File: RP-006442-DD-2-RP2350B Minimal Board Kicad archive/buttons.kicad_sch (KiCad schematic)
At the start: 5 parts, among them SW10 SW_DIP_x08, SW5 SW_Push, SW6 SW_Push, SW7 SW_Push, SW8 SW_Push

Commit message: Update 8-bit switch, footprint, datasheet
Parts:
- SW10: footprint Button_Switch_SMD:SW_DIP_SPSTx08_Slide_Omron_A6S-810x_W8.9mm_P2.54mm -> Button_Switch_SMD:SW_DIP_SPSTx08_Slide_9.78x22.5mm_W8.61mm_P2.54mm
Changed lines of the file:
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@@
 			)
 		)
-		(property "Footprint" "Button_Switch_SMD:SW_DIP_SPSTx08_Slide_Omron_A6S-810x_W8.9mm_P2.54mm"
+		(property "Footprint" "Button_Switch_SMD:SW_DIP_SPSTx08_Slide_9.78x22.5mm_W8.61mm_P2.54mm"
 			(at 135.89 109.22 0)
 			(effects
@@
 			)
 		)
-		(property "Datasheet" "https://jlcpcb.com/api/file/downloadByFileSystemAccessId/8588905267774042112"
+		(property "Datasheet" "https://jlcpcb.com/partdetail/55978-DSIC08LSGET/C54953"
 			(at 135.89 109.22 0)
 			(effects

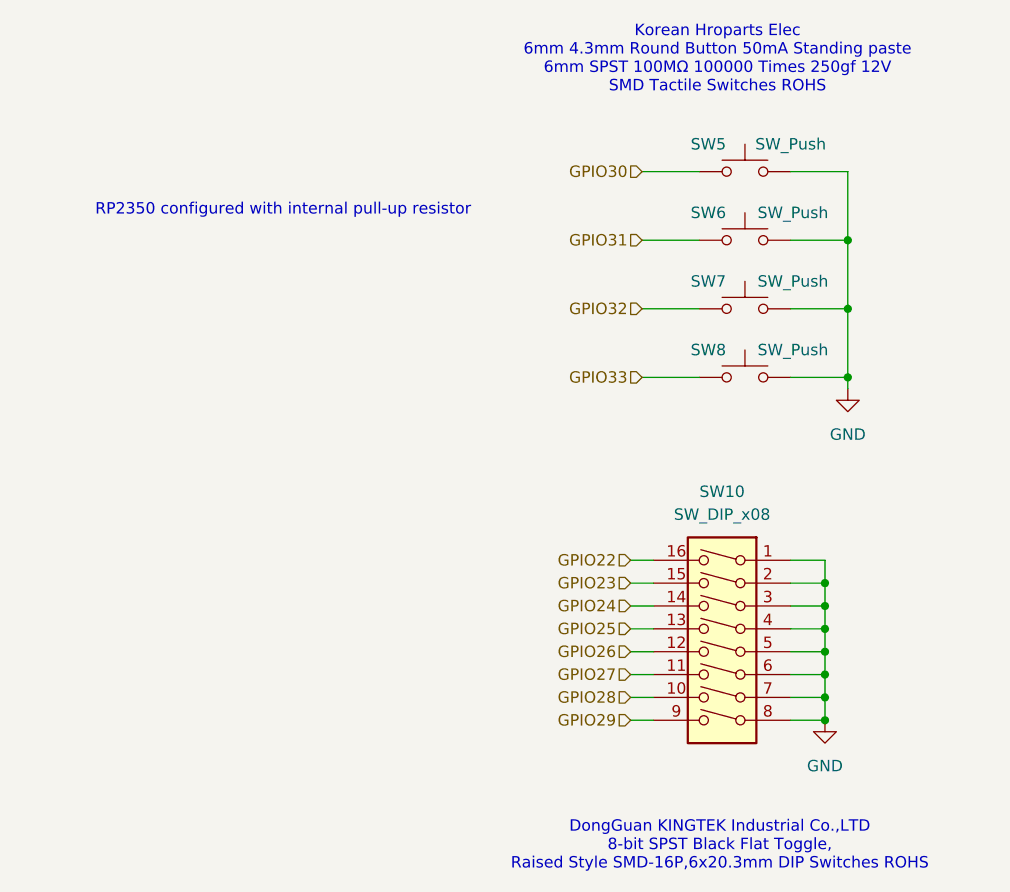
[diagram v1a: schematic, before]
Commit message: Added LCSC numbers to parts
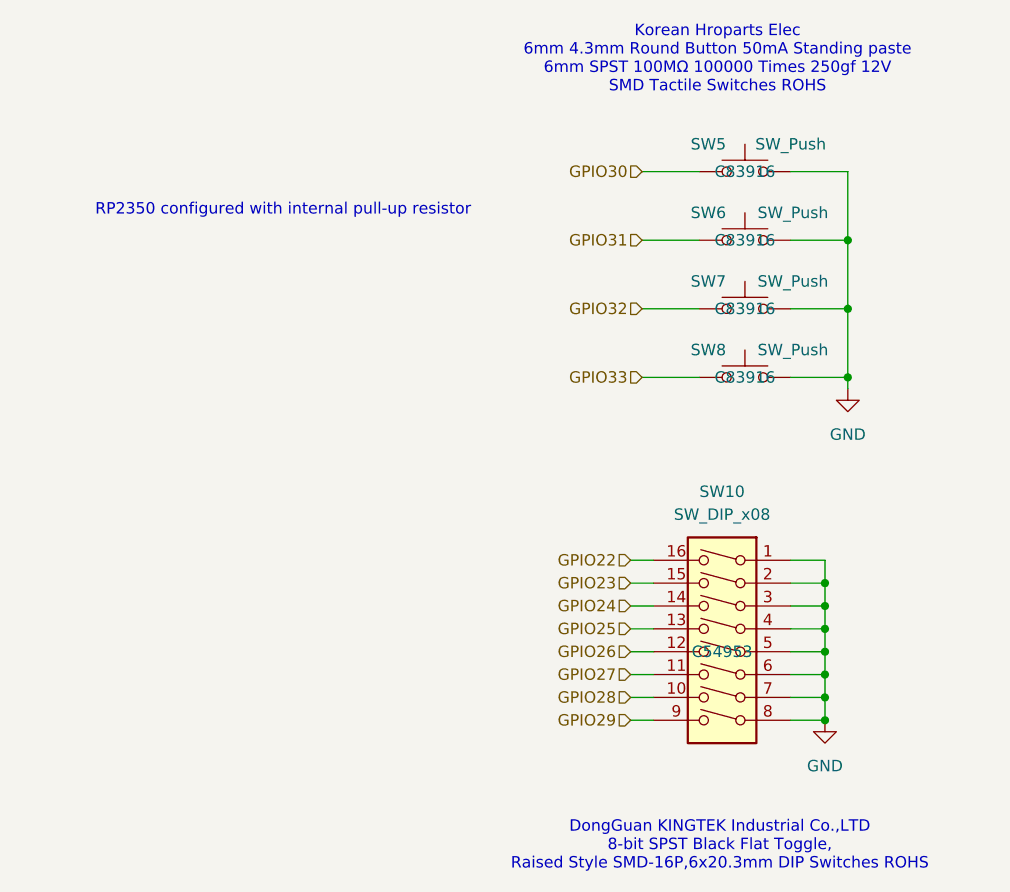
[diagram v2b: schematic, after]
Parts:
- SW10: LCSC (none) -> C54953
- SW5, SW6, SW7, SW8: LCSC (none) -> C83916
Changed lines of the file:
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@@
+			)
+		)
+		(property "LCSC" "C83916"
+			(at 138.43 78.74 0)
+			(effects
+				(font
+					(size 1.27 1.27)
+				)
 			)
 		)
@@
 				)
 				(hide yes)
+			)
+		)
+		(property "LCSC" "C83916"
+			(at 138.43 55.88 0)
+			(effects
+				(font
+					(size 1.27 1.27)
+				)
 			)
 		)
@@
 			)
 		)
+		(property "LCSC" "C83916"
+			(at 138.43 63.5 0)
+			(effects
+				(font
+					(size 1.27 1.27)
+				)
+			)
+		)
 		(pin "1"
 		)
@@
 			)
 		)
+		(property "LCSC" "C54953"
+			(at 135.89 109.22 0)
+			(effects
+				(font
+					(size 1.27 1.27)
+				)
+			)
+		)
 		(pin "1"
 		)
@@
 			)
 		)
+		(property "LCSC" "C83916"
+			(at 138.43 71.12 0)
+			(effects
+				(font
+					(size 1.27 1.27)
+				)
+			)
+		)
